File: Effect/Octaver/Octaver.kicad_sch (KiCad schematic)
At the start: 34 parts, among them J1 Conn_01x04_Pin, J2 Conn_01x04_Pin, Q1 MMBF5103, Q2 DMMT5551, Q3 DMMT5551

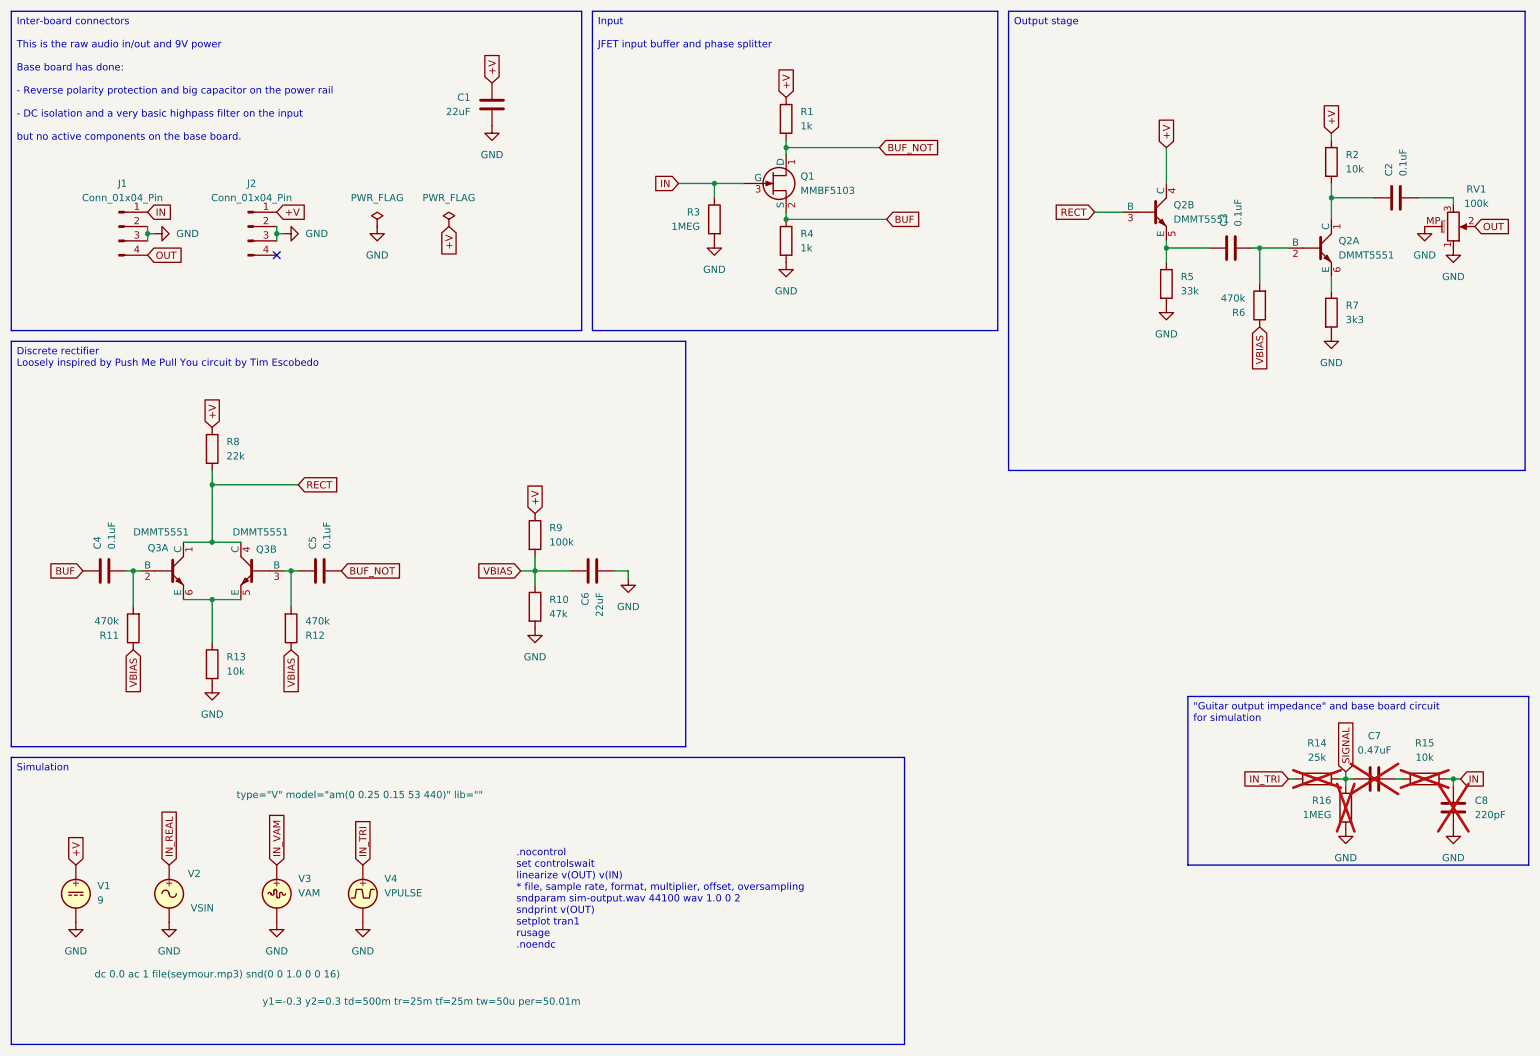
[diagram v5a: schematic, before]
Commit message: Update Octaver for bass frequencies
This is just updating the 0.1uF caps to 1uF, which gives much better
low-frequency behavior.  That does mean replacing the small 0704 form
factor with a 1206 one, so the pcb layout changes a bit.

It also means not using C0G caps, but let's be honest here: audiophile
this is not.

Signed-off-by: Linus Torvalds <torvalds@linux-foundation.org>
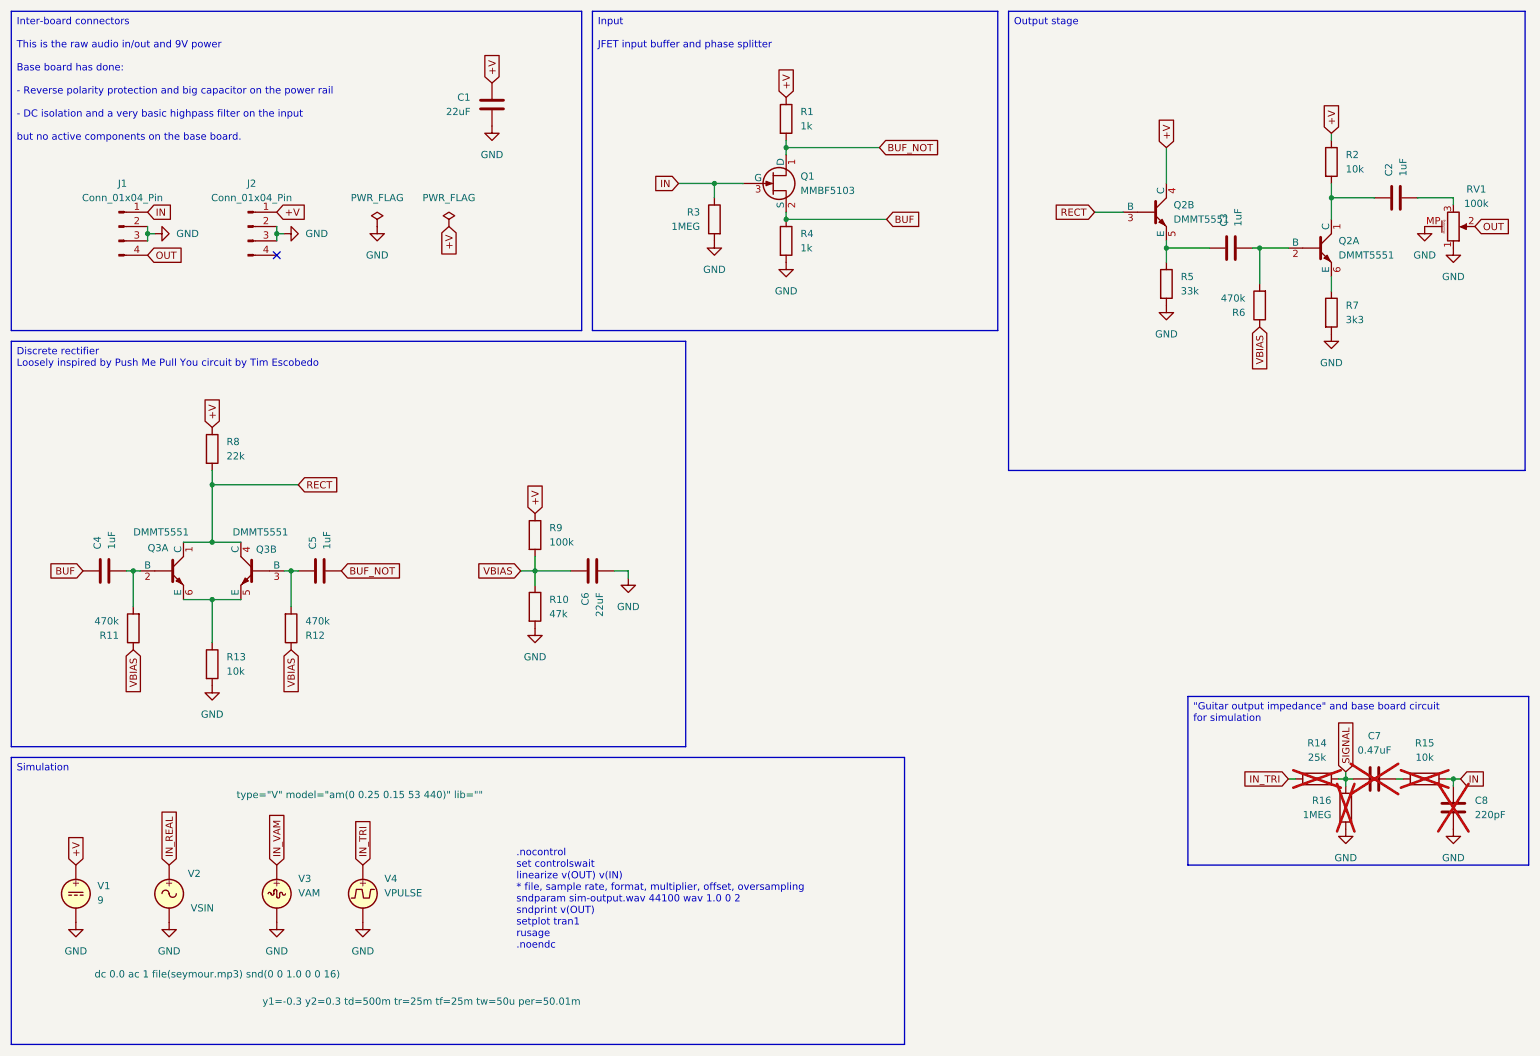
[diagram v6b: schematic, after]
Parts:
- C2, C3, C4, C5: value 0.1uF -> 1uF; footprint Mylib:C_0704_1810Metric -> Capacitor_SMD:C_1206_3216Metric
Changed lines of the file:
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@@
 			)
 		)
-		(property "Value" "0.1uF"
+		(property "Value" "1uF"
 			(at 69.8499 109.22 0)
 			(effects
@@
 			)
 		)
-		(property "Footprint" "Mylib:C_0704_1810Metric"
+		(property "Footprint" "Capacitor_SMD:C_1206_3216Metric"
 			(at 72.39 112.0648 0)
 			(hide yes)
@@
 			)
 		)
-		(property "Value" "0.1uF"
+		(property "Value" "1uF"
 			(at 231.1399 52.07 0)
 			(effects
@@
 			)
 		)
-		(property "Footprint" "Mylib:C_0704_1810Metric"
+		(property "Footprint" "Capacitor_SMD:C_1206_3216Metric"
 			(at 233.68 54.9148 0)
 			(hide yes)
@@
 		(dnp no)
 		(fields_autoplaced yes)
-		(property "Reference" "#PWR024"
+		(property "Reference" "#PWR019"
 			(at 76.2 181.61 0)
 			(hide yes)
@@
 			(project "Octaver"
 				(path "/9e337e0b-885b-4d2b-99a2-62cdd082c615"
-					(reference "#PWR024")
+					(reference "#PWR019")
 					(unit 1)
 				)
@@
 			)
 		)
-		(property "Value" "0.1uF"
+		(property "Value" "1uF"
 			(at 260.3499 43.18 0)
 			(effects
@@
 			)
 		)
-		(property "Footprint" "Mylib:C_0704_1810Metric"
+		(property "Footprint" "Capacitor_SMD:C_1206_3216Metric"
 			(at 262.89 46.0248 0)
 			(hide yes)
@@
 			)
 		)
-		(property "Value" "0.1uF"
+		(property "Value" "1uF"
 			(at 31.7499 109.22 0)
 			(effects
@@
 			)
 		)
-		(property "Footprint" "Mylib:C_0704_1810Metric"
+		(property "Footprint" "Capacitor_SMD:C_1206_3216Metric"
 			(at 34.29 112.0648 0)
 			(hide yes)
